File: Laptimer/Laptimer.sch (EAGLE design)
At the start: 63 parts, among them IC1 MCP73831/OT, IC5 NE555D, Q1 8mhz, Q4 PBSS4120T, X1 mini-usb

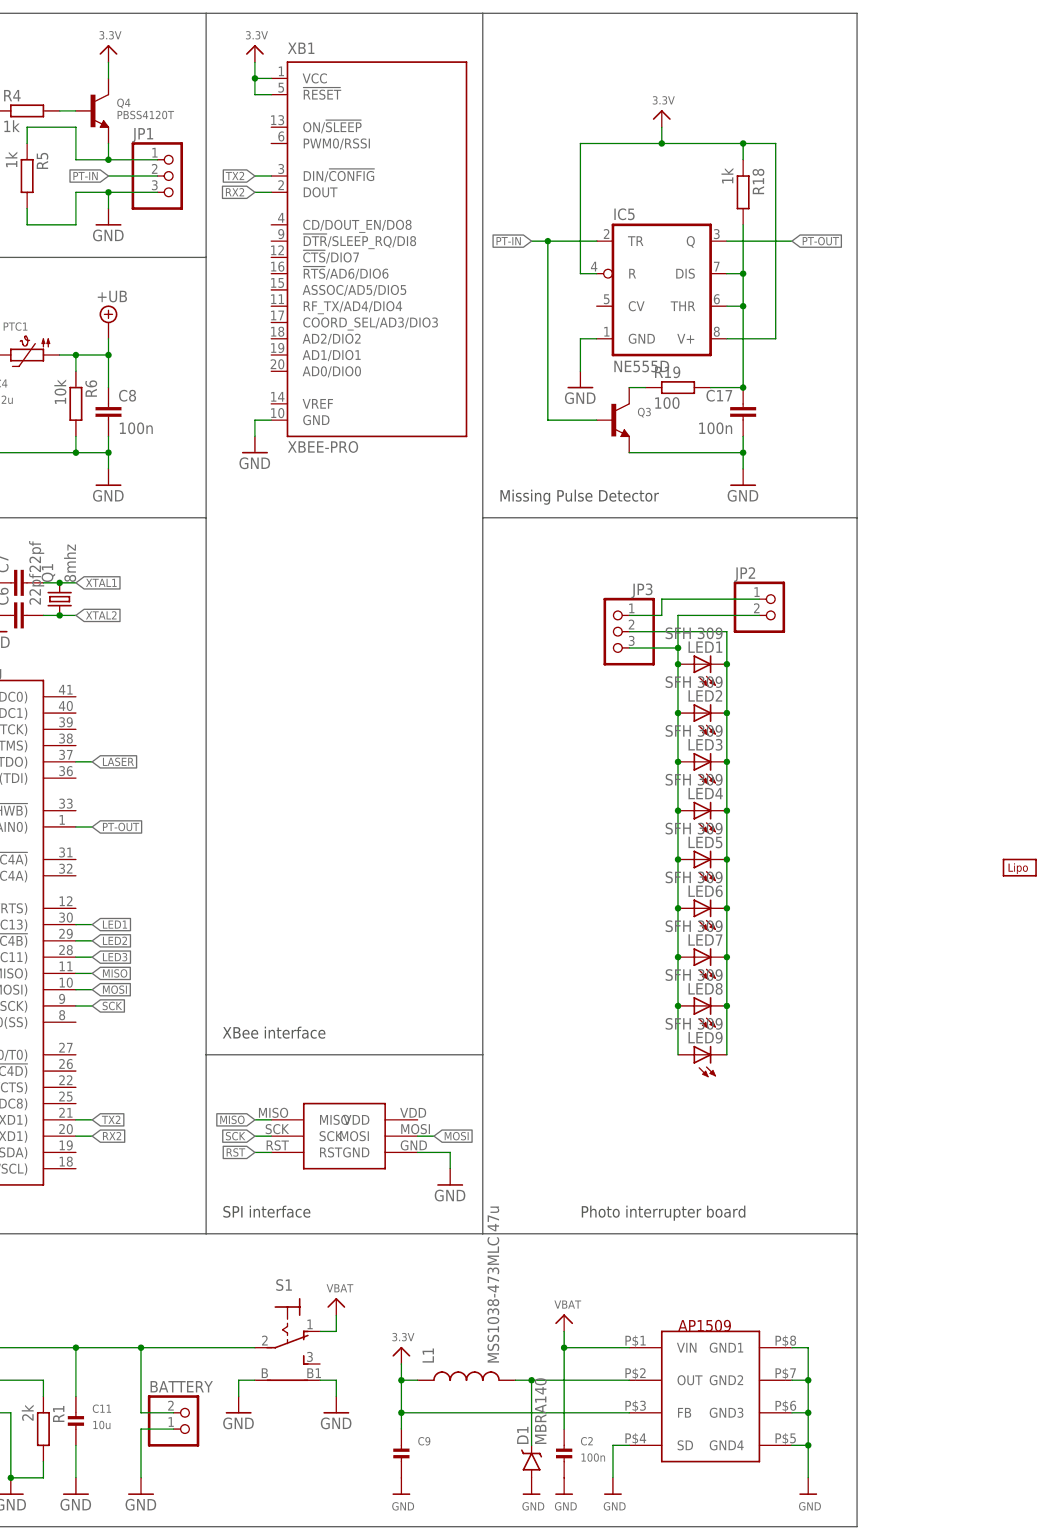
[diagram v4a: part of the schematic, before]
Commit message: added battery and layout changes
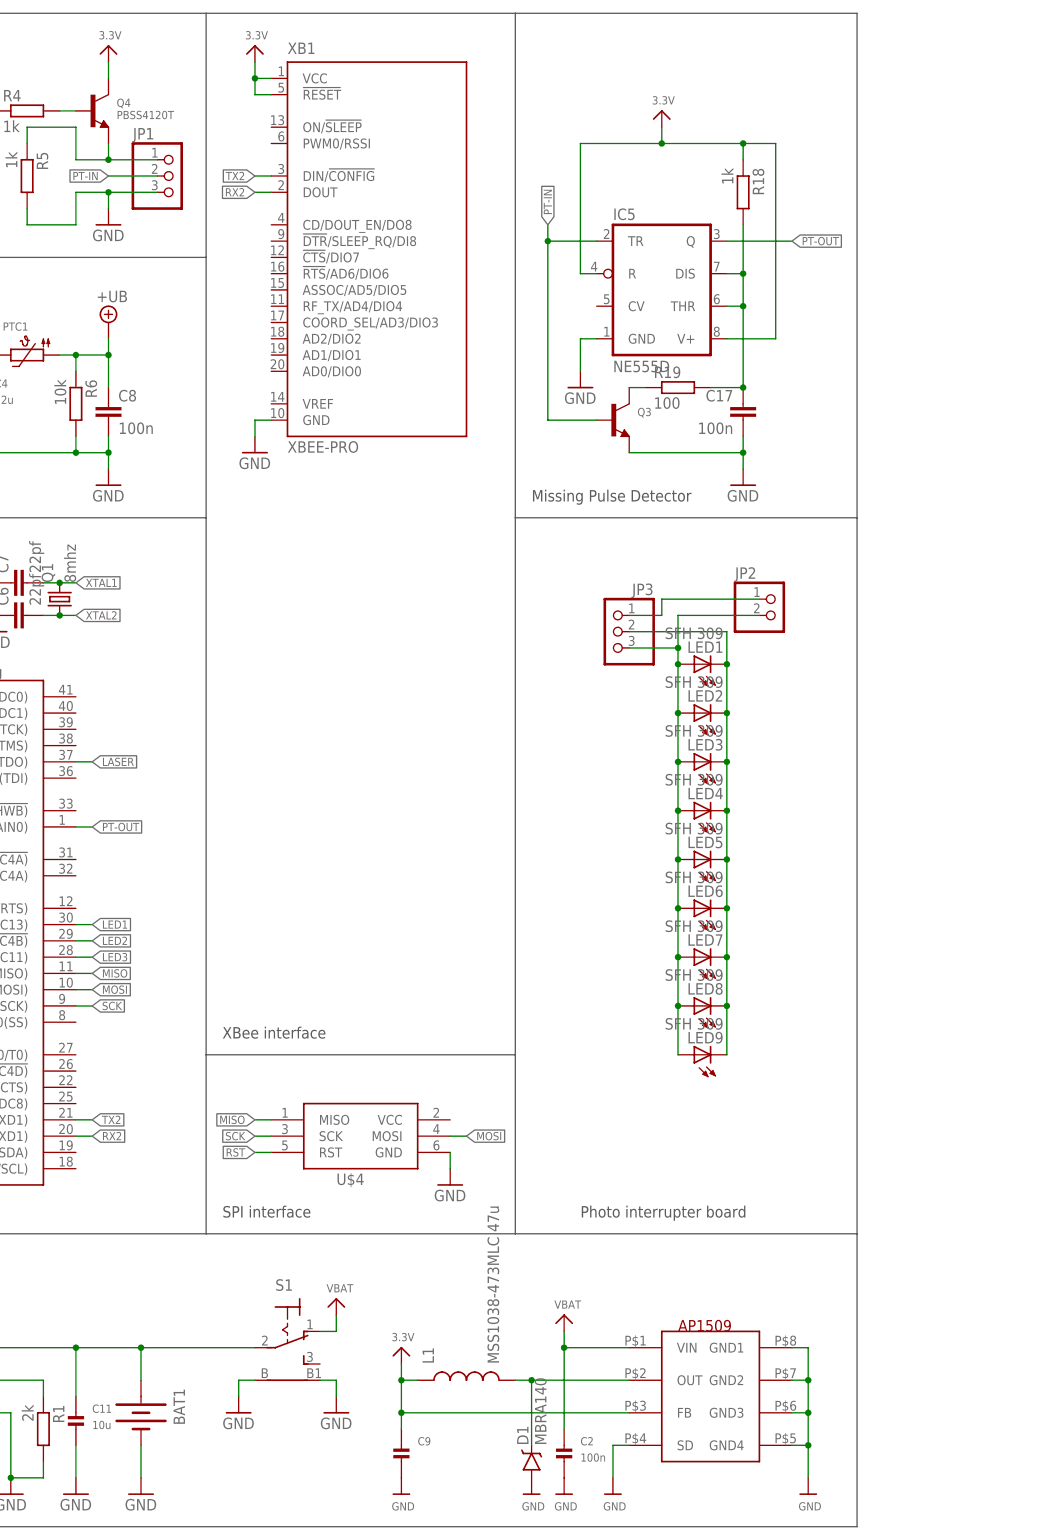
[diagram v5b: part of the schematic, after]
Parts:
- removed BATTERY: (no value), adafruit:JST_2PIN-SMT-RA
- removed U$17: LIPO-OUTLINE2000, SparkFun-Electromechanical:LIPO-OUTLINE2000
- added BAT1: (no value), SparkFun-Electromechanical:BATTERY18650
- U$4: value ISP-HEADER -> AVRISP-BOX; device ISP-Header:ISP-HEADER -> adafruit:AVRISP-BOX
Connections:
- net GND: now also BAT1.-; no longer BATTERY.2
- net N$31: now also BAT1.+; no longer BATTERY.1
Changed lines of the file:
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@@
 <part name="R8" library="rcl" deviceset="R-EU_" device="R0603" value="22"/>
 <part name="R9" library="rcl" deviceset="R-EU_" device="R0603" value="22"/>
-<part name="BATTERY" library="adafruit" deviceset="JST_2PIN" device="-SMT-RA"/>
 <part name="R14" library="rcl" deviceset="R-EU_" device="R0603" value="220"/>
 <part name="R15" library="rcl" deviceset="R-EU_" device="R0603" value="220"/>
@@
 <part name="R3" library="rcl" deviceset="R-EU_" device="R0603" value="1k"/>
 <part name="GND6" library="supply1" deviceset="GND" device=""/>
-<part name="U$4" library="ISP-Header" deviceset="ISP-HEADER" device=""/>
+<part name="U$4" library="adafruit" deviceset="AVRISP" device="-BOX"/>
 <part name="LED1" library="adafruit" deviceset="LED" device="3MM" value="SFH 309"/>
 <part name="LED2" library="adafruit" deviceset="LED" device="3MM" value="SFH 309"/>
@@
 <part name="JP2" library="microbuilder" deviceset="HEADER-1X2" device="ROUND"/>
 <part name="JP1" library="adafruit" deviceset="PINHD-1X3" device=""/>
-<part name="U$17" library="SparkFun-Electromechanical" deviceset="LIPO-OUTLINE" device="2000"/>
+<part name="BAT1" library="SparkFun-Electromechanical" deviceset="BATTERY" device="18650"/>
 </parts>
 <sheets>
@@
 <text x="2.54" y="2.54" size="1.778" layer="97">Power Supply + LiPo Charger</text>
 <wire x1="0" y1="45.72" x2="99.06" y2="45.72" width="0.1524" layer="97"/>
-<wire x1="99.06" y1="45.72" x2="142.24" y2="45.72" width="0.1524" layer="97"/>
+<wire x1="99.06" y1="45.72" x2="147.32" y2="45.72" width="0.1524" layer="97"/>
 <wire x1="0" y1="45.72" x2="0" y2="157.48" width="0.1524" layer="97"/>
 <wire x1="0" y1="157.48" x2="99.06" y2="157.48" width="0.1524" layer="97"/>
-<wire x1="142.24" y1="157.48" x2="142.24" y2="73.66" width="0.1524" layer="97"/>
+<wire x1="147.32" y1="157.48" x2="147.32" y2="73.66" width="0.1524" layer="97"/>
 <text x="2.54" y="48.26" size="1.778" layer="97">ATMEGA 32u4</text>
-<wire x1="142.24" y1="73.66" x2="142.24" y2="45.72" width="0.1524" layer="97"/>
-<wire x1="142.24" y1="157.48" x2="200.66" y2="157.48" width="0.1524" layer="97"/>
+<wire x1="147.32" y1="73.66" x2="147.32" y2="45.72" width="0.1524" layer="97"/>
+<wire x1="147.32" y1="157.48" x2="200.66" y2="157.48" width="0.1524" layer="97"/>
 <wire x1="200.66" y1="157.48" x2="200.66" y2="45.72" width="0.1524" layer="97"/>
 <wire x1="200.66" y1="45.72" x2="200.66" y2="0" width="0.1524" layer="97"/>
@@
 <wire x1="99.06" y1="198.12" x2="99.06" y2="157.48" width="0.1524" layer="97"/>
 <wire x1="200.66" y1="157.48" x2="200.66" y2="236.22" width="0.1524" layer="97"/>
-<wire x1="200.66" y1="236.22" x2="142.24" y2="236.22" width="0.1524" layer="97"/>
-<wire x1="142.24" y1="236.22" x2="142.24" y2="157.48" width="0.1524" layer="97"/>
-<wire x1="142.24" y1="236.22" x2="99.06" y2="236.22" width="0.1524" layer="97"/>
+<wire x1="200.66" y1="236.22" x2="147.32" y2="236.22" width="0.1524" layer="97"/>
+<wire x1="147.32" y1="236.22" x2="147.32" y2="157.48" width="0.1524" layer="97"/>
+<wire x1="147.32" y1="236.22" x2="99.06" y2="236.22" width="0.1524" layer="97"/>
 <wire x1="99.06" y1="236.22" x2="99.06" y2="198.12" width="0.1524" layer="97"/>
 <wire x1="99.06" y1="236.22" x2="53.34" y2="236.22" width="0.1524" layer="97"/>
@@
 <text x="15.24" y="200.66" size="1.778" layer="97">Status LEDS</text>
 <text x="101.6" y="76.2" size="1.778" layer="97">XBee interface</text>
-<text x="144.78" y="160.02" size="1.778" layer="97">Missing Pulse Detector</text>
+<text x="149.86" y="160.02" size="1.778" layer="97">Missing Pulse Detector</text>
 <text x="157.48" y="48.26" size="1.778" layer="97">Photo interrupter board</text>
 <wire x1="53.34" y1="236.22" x2="0" y2="236.22" width="0.1524" layer="97"/>
 <wire x1="0" y1="236.22" x2="0" y2="198.12" width="0.1524" layer="97"/>
-<wire x1="142.24" y1="45.72" x2="200.66" y2="45.72" width="0.1524" layer="97"/>
-<wire x1="142.24" y1="73.66" x2="99.06" y2="73.66" width="0.1524" layer="97"/>
+<wire x1="147.32" y1="45.72" x2="200.66" y2="45.72" width="0.1524" layer="97"/>
+<wire x1="147.32" y1="73.66" x2="99.06" y2="73.66" width="0.1524" layer="97"/>
 <wire x1="99.06" y1="73.66" x2="99.06" y2="157.48" width="0.1524" layer="97"/>
 <wire x1="99.06" y1="73.66" x2="99.06" y2="45.72" width="0.1524" layer="97"/>
@@
 <instance part="R8" gate="G$1" x="50.8" y="180.34" rot="R180"/>
 <instance part="R9" gate="G$1" x="50.8" y="172.72" rot="R180"/>
-<instance part="BATTERY" gate="G$1" x="96.52" y="15.24"/>
 <instance part="R14" gate="G$1" x="25.4" y="215.9"/>
 <instance part="R15" gate="G$1" x="25.4" y="220.98"/>
@@
 <instance part="R3" gate="G$1" x="30.48" y="10.16"/>
 <instance part="GND6" gate="1" x="137.16" y="53.34"/>
-<instance part="U$4" gate="G$1" x="119.38" y="63.5"/>
+<instance part="U$4" gate="G$1" x="121.92" y="60.96"/>
 <instance part="LED1" gate="G$1" x="175.26" y="134.62" rot="R90"/>
 <instance part="LED2" gate="G$1" x="175.26" y="127" rot="R90"/>
@@
 <instance part="JP2" gate="G$1" x="187.96" y="142.24"/>
 <instance part="JP1" gate="A" x="93.98" y="210.82"/>
-<instance part="U$17" gate="G$1" x="223.52" y="101.6"/>
+<instance part="BAT1" gate="G$1" x="88.9" y="17.78" rot="R270"/>
 </instances>
 <busses>
@@
 </segment>
 <segment>
-<pinref part="GND2" gate="1" pin="GND"/>
-<wire x1="88.9" y1="15.24" x2="88.9" y2="7.62" width="0.1524" layer="91"/>
-<pinref part="BATTERY" gate="G$1" pin="2"/>
-<wire x1="88.9" y1="15.24" x2="93.98" y2="15.24" width="0.1524" layer="91"/>
-</segment>
-<segment>
 <pinref part="IC1" gate="G$1" pin="VSS"/>
 <pinref part="GND1" gate="1" pin="GND"/>
@@
 <segment>
 <pinref part="GND6" gate="1" pin="GND"/>
-<wire x1="137.16" y1="58.42" x2="137.16" y2="55.88" width="0.1524" layer="91"/>
 <pinref part="U$4" gate="G$1" pin="GND"/>
-<wire x1="137.16" y1="58.42" x2="132.08" y2="58.42" width="0.1524" layer="91"/>
+<wire x1="137.16" y1="55.88" x2="137.16" y2="58.42" width="0.1524" layer="91"/>
 </segment>
 <segment>
@@
 <wire x1="119.38" y1="22.86" x2="119.38" y2="20.32" width="0.1524" layer="91"/>
 </segment>
+<segment>
+<pinref part="BAT1" gate="G$1" pin="-"/>
+<pinref part="GND2" gate="1" pin="GND"/>
+<wire x1="88.9" y1="12.7" x2="88.9" y2="7.62" width="0.1524" layer="91"/>
+</segment>
 </net>
 <net name="XTAL2" class="0">
@@
 <net name="N$31" class="0">
 <segment>
-<wire x1="88.9" y1="27.94" x2="88.9" y2="17.78" width="0.1524" layer="91"/>
-<pinref part="BATTERY" gate="G$1" pin="1"/>
-<wire x1="93.98" y1="17.78" x2="88.9" y2="17.78" width="0.1524" layer="91"/>
 <pinref part="IC1" gate="G$1" pin="VBAT"/>
 <wire x1="66.04" y1="27.94" x2="78.74" y2="27.94" width="0.1524" layer="91"/>
 <wire x1="78.74" y1="27.94" x2="88.9" y2="27.94" width="0.1524" layer="91"/>
+<pinref part="C11" gate="G$1" pin="P$1"/>
 <wire x1="88.9" y1="27.94" x2="106.68" y2="27.94" width="0.1524" layer="91"/>
-<junction x="88.9" y="27.94"/>
-<pinref part="C11" gate="G$1" pin="P$1"/>
 <wire x1="78.74" y1="27.94" x2="78.74" y2="20.32" width="0.1524" layer="91"/>
 <junction x="78.74" y="27.94"/>
 <pinref part="S1" gate="1" pin="P"/>
+<pinref part="BAT1" gate="G$1" pin="+"/>
+<wire x1="88.9" y1="27.94" x2="88.9" y2="22.86" width="0.1524" layer="91"/>
+<junction x="88.9" y="27.94"/>
 </segment>
 </net>
@@
 <net name="MOSI" class="0">
 <segment>
-<wire x1="132.08" y1="60.96" x2="134.62" y2="60.96" width="0.1524" layer="91"/>
-<label x="134.62" y="60.96" size="1.27" layer="95" xref="yes"/>
+<wire x1="137.16" y1="60.96" x2="139.7" y2="60.96" width="0.1524" layer="91"/>
+<label x="139.7" y="60.96" size="1.27" layer="95" xref="yes"/>
 <pinref part="U$4" gate="G$1" pin="MOSI"/>
 </segment>
@@
 <pinref part="IC5" gate="A" pin="TR"/>
 <pinref part="Q3" gate="G$1" pin="B"/>
-<wire x1="149.86" y1="200.66" x2="152.4" y2="200.66" width="0.1524" layer="91"/>
+<wire x1="152.4" y1="203.2" x2="152.4" y2="200.66" width="0.1524" layer="91"/>
 <wire x1="152.4" y1="200.66" x2="160.02" y2="200.66" width="0.1524" layer="91"/>
 <wire x1="160.02" y1="172.72" x2="152.4" y2="172.72" width="0.1524" layer="91"/>
 <wire x1="152.4" y1="172.72" x2="152.4" y2="200.66" width="0.1524" layer="91"/>
 <junction x="152.4" y="200.66"/>
-<label x="149.86" y="200.66" size="1.27" layer="95" rot="R180" xref="yes"/>
-</segment>
-</net>
+<label x="152.4" y="203.2" size="1.27" layer="95" rot="R90" xref="yes"/>
+</segment>
+</net>

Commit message: library updates and layout updates
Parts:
- added H1, H2: MOUNT-HOLE3.0, holes:MOUNT-HOLE3.0
- S1: value (none) -> TL36WO; device switch:LPV-1 -> switch:TL36WO
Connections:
- net GND: no longer S1.B, S1.B1
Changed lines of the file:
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@@
 <part name="GND8" library="supply1" deviceset="GND" device=""/>
 <part name="U$20" library="microbuilder" deviceset="3.3V" device=""/>
-<part name="S1" library="switch" deviceset="LPV-1" device=""/>
-<part name="GND10" library="supply1" deviceset="GND" device=""/>
-<part name="GND11" library="supply1" deviceset="GND" device=""/>
 <part name="LED9" library="adafruit" deviceset="LED" device="3MM" value="SFH 309"/>
 <part name="JP3" library="adafruit" deviceset="PINHD-1X3" device=""/>
@@
 <part name="JP1" library="adafruit" deviceset="PINHD-1X3" device=""/>
 <part name="BAT1" library="SparkFun-Electromechanical" deviceset="BATTERY" device="18650"/>
+<part name="H1" library="holes" deviceset="MOUNT-HOLE" device="3.0"/>
+<part name="H2" library="holes" deviceset="MOUNT-HOLE" device="3.0"/>
+<part name="S1" library="switch" deviceset="TL36WO" device=""/>
 </parts>
 <sheets>
@@
 <instance part="GND8" gate="1" x="43.18" y="205.74"/>
 <instance part="U$20" gate="G$1" x="17.78" y="231.14"/>
-<instance part="S1" gate="1" x="111.76" y="30.48" rot="R270"/>
-<instance part="GND10" gate="1" x="104.14" y="17.78"/>
-<instance part="GND11" gate="1" x="119.38" y="17.78"/>
 <instance part="LED9" gate="G$1" x="175.26" y="73.66" rot="R90"/>
 <instance part="JP3" gate="A" x="162.56" y="139.7" rot="MR0"/>
@@
 <instance part="JP1" gate="A" x="93.98" y="210.82"/>
 <instance part="BAT1" gate="G$1" x="88.9" y="17.78" rot="R270"/>
+<instance part="H1" gate="G$1" x="-25.4" y="152.4"/>
+<instance part="H2" gate="G$1" x="-25.4" y="144.78"/>
+<instance part="S1" gate="BEF1" x="111.76" y="27.94" rot="R270"/>
 </instances>
 <busses>
@@
 </segment>
 <segment>
-<pinref part="S1" gate="1" pin="B"/>
-<pinref part="GND10" gate="1" pin="GND"/>
-<wire x1="106.68" y1="22.86" x2="104.14" y2="22.86" width="0.1524" layer="91"/>
-<wire x1="104.14" y1="22.86" x2="104.14" y2="20.32" width="0.1524" layer="91"/>
-</segment>
-<segment>
-<pinref part="S1" gate="1" pin="B1"/>
-<pinref part="GND11" gate="1" pin="GND"/>
-<wire x1="116.84" y1="22.86" x2="119.38" y2="22.86" width="0.1524" layer="91"/>
-<wire x1="119.38" y1="22.86" x2="119.38" y2="20.32" width="0.1524" layer="91"/>
-</segment>
-<segment>
 <pinref part="BAT1" gate="G$1" pin="-"/>
 <pinref part="GND2" gate="1" pin="GND"/>
@@
 <wire x1="78.74" y1="27.94" x2="78.74" y2="20.32" width="0.1524" layer="91"/>
 <junction x="78.74" y="27.94"/>
-<pinref part="S1" gate="1" pin="P"/>
 <pinref part="BAT1" gate="G$1" pin="+"/>
 <wire x1="88.9" y1="27.94" x2="88.9" y2="22.86" width="0.1524" layer="91"/>
 <junction x="88.9" y="27.94"/>
+<pinref part="S1" gate="BEF1" pin="P"/>
 </segment>
 </net>
@@
 <wire x1="119.38" y1="30.48" x2="119.38" y2="33.02" width="0.1524" layer="91"/>
 <pinref part="U$13" gate="G$1" pin="VBAT"/>
-<pinref part="S1" gate="1" pin="O"/>
 <wire x1="116.84" y1="30.48" x2="119.38" y2="30.48" width="0.1524" layer="91"/>
-</segment>
-</net>
+<pinref part="S1" gate="BEF1" pin="O"/>
+</segment>
+</net>

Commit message: preperations for etching
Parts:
- removed PTC1: (no value), microbuilder:PTC1812
- added PTC2: (no value), microbuilder:PTC1206
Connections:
- net +UB: now also PTC2.1; no longer PTC1.1
- net N$13: now also PTC2.2; no longer PTC1.2
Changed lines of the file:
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@@
 <part name="C5" library="microbuilder" deviceset="CAP_CERAMIC" device="_0805MP" value="1u"/>
 <part name="GND4" library="supply1" deviceset="GND" device=""/>
-<part name="PTC1" library="microbuilder" deviceset="PTC" device="1812"/>
 <part name="R6" library="rcl" deviceset="R-EU_" device="R0603" value="10k"/>
 <part name="C8" library="rcl" deviceset="C-EU" device="C0603K" value="100n"/>
@@
 <part name="H2" library="holes" deviceset="MOUNT-HOLE" device="3.0"/>
 <part name="S1" library="switch" deviceset="TL36WO" device=""/>
+<part name="PTC2" library="microbuilder" deviceset="PTC" device="1206"/>
 </parts>
 <sheets>
@@
 <instance part="C5" gate="G$1" x="7.62" y="101.6" rot="R180"/>
 <instance part="GND4" gate="1" x="7.62" y="93.98"/>
-<instance part="PTC1" gate="G$1" x="71.12" y="182.88"/>
 <instance part="R6" gate="G$1" x="78.74" y="175.26" rot="R270"/>
 <instance part="C8" gate="G$1" x="83.82" y="175.26"/>
@@
 <instance part="H2" gate="G$1" x="-25.4" y="144.78"/>
 <instance part="S1" gate="BEF1" x="111.76" y="27.94" rot="R270"/>
+<instance part="PTC2" gate="G$1" x="71.12" y="182.88"/>
 </instances>
 <busses>
@@
 <net name="+UB" class="0">
 <segment>
-<pinref part="PTC1" gate="G$1" pin="1"/>
 <pinref part="R6" gate="G$1" pin="1"/>
 <wire x1="76.2" y1="182.88" x2="78.74" y2="182.88" width="0.1524" layer="91"/>
@@
 <wire x1="83.82" y1="185.42" x2="83.82" y2="182.88" width="0.1524" layer="91"/>
 <junction x="83.82" y="182.88"/>
+<pinref part="PTC2" gate="G$1" pin="1"/>
 </segment>
 <segment>
@@
 <pinref part="X1" gate="G$1" pin="1"/>
 <wire x1="63.5" y1="182.88" x2="40.64" y2="182.88" width="0.1524" layer="91"/>
-<pinref part="PTC1" gate="G$1" pin="2"/>
 <wire x1="63.5" y1="182.88" x2="66.04" y2="182.88" width="0.1524" layer="91"/>
 <junction x="63.5" y="182.88"/>
-</segment>
-</net>
+<pinref part="PTC2" gate="G$1" pin="2"/>
+</segment>
+</net>

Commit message: power supply update
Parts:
- removed D1: MBRA140, SparkFun-DiscreteSemi:MBRA140
- removed L1: MSS1038-473MLC 47u, SparkFun-Passives:INDUCTORPWR
- removed U$2: AP1509, unicorn_v2:AP1509
- added U1: ADP124ARHZ-3.3-R7, Analog Devices_By_element14_Batch_1:ADP124ARHZ-3.3-R7
- C2: value 100n -> 1u; device microbuilder:CAP_CERAMIC_0603MP -> microbuilder:CAP_CERAMIC_0805MP
- C9: value (none) -> 1u
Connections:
- removed net VBAT: C2.P$1, S1.O, U$2.VIN
- net 3.3V: now also U1.VOUT, U1.VOUT_2, U1.VOUT_SENSE; no longer L1.1, U$2.FB
- net GND: now also C2.P$1, U1.EP, U1.GND; no longer C2.P$2, D1.A, U$2.GND1, U$2.GND2, U$2.GND3, U$2.GND4, U$2.SD
- net N$17: now also C2.P$2, S1.O, U1.EN, U1.VIN, U1.VIN_2; no longer D1.C, L1.2, U$2.OUT
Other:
- moved on the sheet: C2, C9
